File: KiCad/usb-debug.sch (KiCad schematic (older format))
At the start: 76 parts, among them IC15 TLV70018DCKT, IC16 NCP380HSNAJAAT1G, IC7 HD3SS3220, J11 632723300011, Q1 PMV32UP, T6 BSS138APW

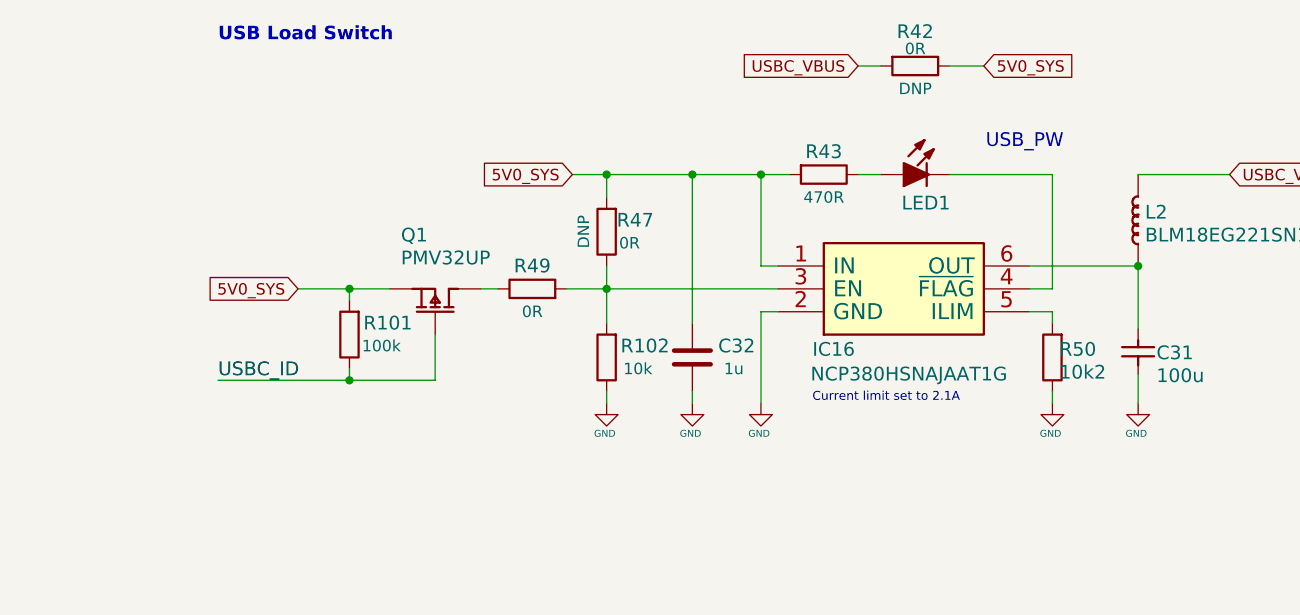
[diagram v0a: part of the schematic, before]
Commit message: Replace NCP380HS with AP22652W6-7
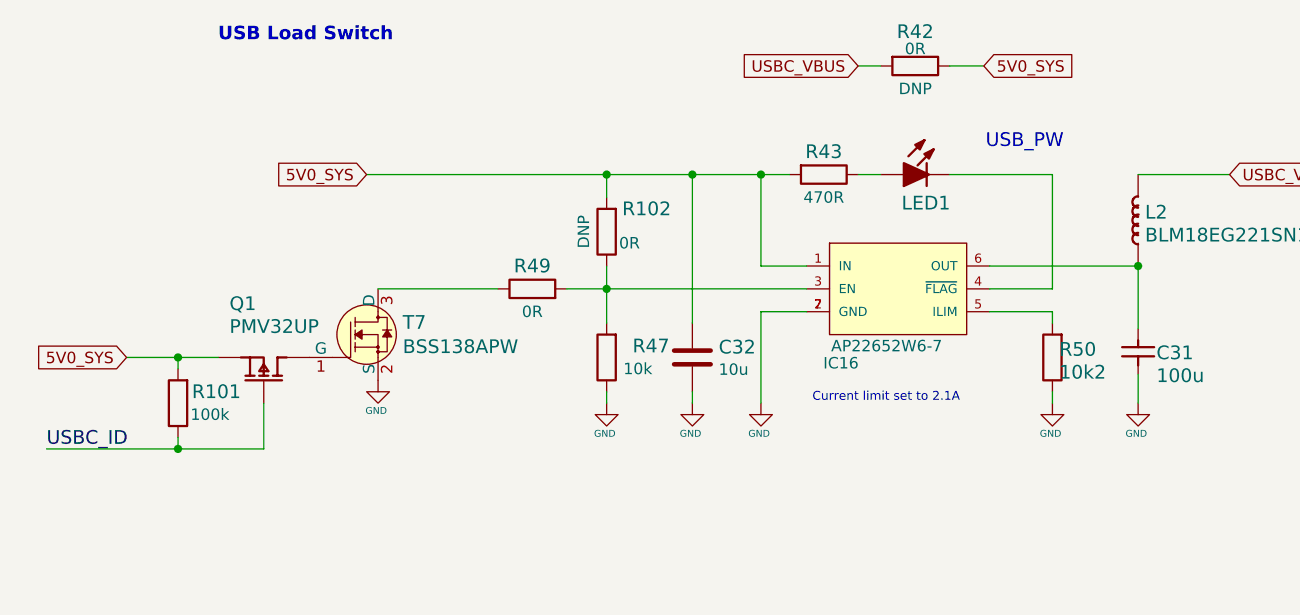
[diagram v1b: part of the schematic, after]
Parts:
- removed C32: C_1u_0402, jetson-nano-baseboard-footprints:0402-cap, symbol jetson-nano-baseboard:C_1u_0402
- removed IC16: NCP380HSNAJAAT1G, jetson-nano-baseboard-footprints:TSOP-6, symbol jetson-nano-baseboard:NCP380HSNAJAAT1G
- added C32: C_10u_0402, antmicro-footprints:0402-cap, symbol antmicroCapacitors0402:C_10u_0402
- added IC16: AP22652W6-7, antmicro-footprints:SOT-23-6, symbol antmicroPMICPowerDistributionSwitchesLoadDrivers:AP22652W6-7
- added T7: BSS138APW, jetson-nano-baseboard-footprints:SC70-3, symbol jetson-nano-baseboard:BSS138APW
- renumbered R47 to R102, R102 to R47
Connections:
- net 5V0_SYS: now also C32.1, IC16.1 (IN)
- net GND: now also C32.2, IC16.2 (GND), IC16.7 (GND), T7.2 (S)
- net at R50.2: now also IC16.5 (ILIM)
- net at C31.2, L2.1 (P): now also IC16.6 (OUT)
- net at Q1.3 (D): now also T7.1 (G); no longer R49.1
- net at LED1.K: now also IC16.4 (~FLAG~)
- net at R102.1, R47.2, R49.2: now also IC16.3 (EN)
- new net: R49.1, T7.3 (D)
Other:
- moved on the sheet: Q1, R101
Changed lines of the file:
@@
 Text Notes 4108 8992 0    60   ~ 0
 USB_PW
-Text Label 750  10000 0    60   ~ 0
+Text Label 0    10300 0    60   ~ 0
 USBC_ID
 Text Label 12600 5075 1    70   ~ 0
@@
 Text Label 4500 5650 0    60   ~ 0
 OTG_USB_VBUS
-Text GLabel 1100 9600 0    50   Input ~ 0
+Text GLabel 350  9900 0    50   Input ~ 0
 5V0_SYS
-Text GLabel 2300 9100 0    50   Input ~ 0
+Text GLabel 1400 9100 0    50   Input ~ 0
 5V0_SYS
 Text GLabel 5175 9100 2    50   Input ~ 0
@@
 $EndComp
 $Comp
-L jetson-nano-baseboard:NCP380HSNAJAAT1G IC16
-U 1 1 5E710326
-P 3800 9600
-F 0 "IC16" H 3350 9300 60  0000 L BNN
-F 1 "NCP380HSNAJAAT1G" H 3342 9192 60  0000 L BNN
-F 2 "jetson-nano-baseboard-footprints:TSOP-6" H 3350 9100 60  0001 C CNN
-F 3 "" H 3350 9100 60  0001 C CNN
-F 4 "ON Semiconductor" V 1400 8707 60  0001 C CNN "Manufacturer"
-F 5 "NCP380HSNAJAAT1G" H -34116 -14968 50  0001 C CNN "MPN"
-	1    3800 9600
-	1    0    0    -1
-$EndComp
-$Comp
 L jetson-nano-baseboard:LED LED1
 U 1 1 5E710325
@@
 L jetson-nano-baseboard:PMOS Q1
 U 1 1 5E710318
-P 1700 9600
-F 0 "Q1" V 1900 9750 60  0000 R TNN
-F 1 "PMV32UP" V 1800 9750 60  0000 R TNN
-F 2 "jetson-nano-baseboard-footprints:SOT-23s" H 1800 9750 60  0001 C CNN
-F 3 "" H 1800 9750 60  0001 C CNN
-F 4 "PMV32UP" H -34116 -14968 50  0001 C CNN "MPN"
-F 5 "NXP" H -34116 -14968 50  0001 C CNN "Manufacturer"
-	1    1700 9600
+P 950 9900
+F 0 "Q1" V 1150 10050 60  0000 R TNN
+F 1 "PMV32UP" V 1050 10050 60  0000 R TNN
+F 2 "jetson-nano-baseboard-footprints:SOT-23s" H 1050 10050 60  0001 C CNN
+F 3 "" H 1050 10050 60  0001 C CNN
+F 4 "PMV32UP" H -34866 -14668 50  0001 C CNN "MPN"
+F 5 "NXP" H -34866 -14668 50  0001 C CNN "Manufacturer"
+	1    950  9900
 	0    -1   -1   0
 $EndComp
@@
 	5725 5950 5575 5950
 Wire Wire Line
-	1700 10000 1700 9800
-Wire Wire Line
-	3200 9700 3125 9700
+	950  10300 950  10100
 Wire Wire Line
 	3125 9700 3125 10100
 Connection ~ 2450 9600
-Wire Wire Line
-	2450 9600 3200 9600
-Wire Wire Line
-	2300 9100 2450 9100
 Connection ~ 2450 9100
-Wire Wire Line
-	3200 9500 3125 9500
 Wire Wire Line
 	3125 9500 3125 9100
 Connection ~ 3125 9100
-Wire Wire Line
-	4300 9600 4400 9600
 Wire Wire Line
 	4400 9600 4400 9100
@@
 $EndComp
 Wire Wire Line
-	4300 9700 4400 9700
-Wire Wire Line
 	4775 9975 4775 10100
-Wire Wire Line
-	4300 9500 4775 9500
 Wire Wire Line
 	4775 9500 4775 9775
@@
 L jetson-nano-baseboard:R_100k_0402 R101
 U 1 1 629AECD1
-P 1325 9800
-F 0 "R101" V 1375 9525 60  0000 L CNN
-F 1 "R_100k_0402" H 1325 9650 60  0001 C CNN
-F 2 "jetson-nano-baseboard-footprints:0402-res" H 1525 10000 60  0001 L CNN
-F 3 "" H 1325 9800 50  0001 C CNN
-F 4 "VISHAY" H 1525 10200 60  0001 L CNN "Manufacturer"
-F 5 "CRCW0402100KFKEDHP" H 1525 10100 60  0001 L CNN "MPN"
-F 6 "100k" V 1275 9575 50  0000 L CNN "Val"
-	1    1325 9800
+P 575 10100
+F 0 "R101" V 625 9825 60  0000 L CNN
+F 1 "R_100k_0402" H 575 9950 60  0001 C CNN
+F 2 "jetson-nano-baseboard-footprints:0402-res" H 775 10300 60  0001 L CNN
+F 3 "" H 575 10100 50  0001 C CNN
+F 4 "VISHAY" H 775 10500 60  0001 L CNN "Manufacturer"
+F 5 "CRCW0402100KFKEDHP" H 775 10400 60  0001 L CNN "MPN"
+F 6 "100k" V 525 9875 50  0000 L CNN "Val"
+	1    575  10100
 	0    -1   -1   0
 $EndComp
 Wire Wire Line
-	750  10000 1325 10000
-Wire Wire Line
-	1100 9600 1325 9600
-Wire Wire Line
-	1325 9950 1325 10000
-Connection ~ 1325 10000
-Wire Wire Line
-	1325 10000 1700 10000
-Wire Wire Line
-	1325 9650 1325 9600
-Connection ~ 1325 9600
-Wire Wire Line
-	1325 9600 1500 9600
+	0    10300 575  10300
+Wire Wire Line
+	350  9900 575  9900
+Wire Wire Line
+	575  10250 575  10300
+Connection ~ 575  10300
+Wire Wire Line
+	575  10300 950  10300
+Wire Wire Line
+	575  9950 575  9900
+Connection ~ 575  9900
+Wire Wire Line
+	575  9900 750  9900
 $Comp
 L jetson-nano-baseboard:R_0R_0402 R49
@@
 Wire Wire Line
 	2275 9600 2450 9600
-Wire Wire Line
-	1900 9600 1975 9600
-$Comp
-L jetson-nano-baseboard:R_10k_0402 R102
-U 1 1 62A1B644
-P 2450 9900
-F 0 "R102" V 2500 9625 60  0000 L CNN
-F 1 "R_10k_0402" H 2450 9750 60  0001 C CNN
-F 2 "jetson-nano-baseboard-footprints:0402-res" H 2650 10100 60  0001 L CNN
-F 3 "" H 2450 9900 50  0001 C CNN
-F 4 "VISHAY" H 2650 10300 60  0001 L CNN "Manufacturer"
-F 5 "CRCW040210K0FKEDHP" H 2650 10200 60  0001 L CNN "MPN"
-F 6 "10k" V 2400 9700 50  0000 L CNN "Val"
-	1    2450 9900
-	0    -1   -1   0
-$EndComp
-$Comp
-L jetson-nano-baseboard:C_1u_0402 C32
-U 1 1 62A1DA70
-P 2825 9900
-F 0 "C32" H 2550 9850 60  0000 L CNN
-F 1 "C_1u_0402" H 2825 9750 60  0001 C CNN
-F 2 "jetson-nano-baseboard-footprints:0402-cap" H 3025 10100 60  0001 L CNN
-F 3 "" H 2825 9900 50  0001 C CNN
-F 4 "TDK" H 3025 10300 60  0001 L CNN "Manufacturer"
-F 5 "C1005X6S1A105K050BC" H 3025 10200 60  0001 L CNN "MPN"
-F 6 "1u" H 2600 9950 50  0000 L CNN "Val"
-	1    2825 9900
-	-1   0    0    1
-$EndComp
 $Comp
 L jetson-nano-baseboard:GND #GND_0102
@@
 Wire Wire Line
 	2450 9600 2450 9750
-Wire Wire Line
-	2450 10050 2450 10100
-$Comp
-L jetson-nano-baseboard:R_0R_0402 R47
-U 1 1 62A9631F
-P 2450 9350
-F 0 "R47" V 2500 9225 60  0000 C CNN
-F 1 "R_0R_0402" H 2450 9200 60  0001 C CNN
-F 2 "jetson-nano-baseboard-footprints:0402-res" H 2650 9550 60  0001 L CNN
-F 3 "" H 2450 9350 50  0001 C CNN
-F 4 "PANASONIC" H 2650 9750 60  0001 L CNN "Manufacturer"
-F 5 "ERJ2GE0R00X" H 2650 9650 60  0001 L CNN "MPN"
-F 6 "0R" V 2400 9250 50  0000 C CNN "Val"
-F 7 "DNP" H 2450 9450 50  0000 C CNN "DNP"
-	1    2450 9350
-	0    -1   -1   0
-$EndComp
 Wire Wire Line
 	2450 9100 2450 9200
@@
 Wire Wire Line
 	4400 10100 4400 10050
+Wire Wire Line
+	1450 9600 1975 9600
+$Comp
+L jetson-nano-baseboard:GND #GND_0152
+U 1 1 61861FAC
+P 1450 10000
+F 0 "#GND_0152" H 1450 10000 20  0001 C CNN
+F 1 "GND" H 1442 9867 30  0000 C CNN
+F 2 "" H 1450 10000 70  0001 C CNN
+F 3 "" H 1450 10000 70  0001 C CNN
+	1    1450 10000
+	1    0    0    -1
+$EndComp
+Wire Wire Line
+	1400 9100 2450 9100
+$Comp
+L jetson-nano-baseboard:BSS138APW T?
+U 1 1 617C458B
+P 1450 9800
+AR Path="/608DC6E9/617C458B" Ref="T?"  Part="1"
+AR Path="/608DF3E5/617C458B" Ref="T7"  Part="1"
+F 0 "T7" H 1558 9853 60  0000 L CNN
+F 1 "BSS138APW" H 1558 9747 60  0000 L CNN
+F 2 "jetson-nano-baseboard-footprints:SC70-3" H 1650 10000 60  0001 L CNN
+F 3 "" H 1650 10100 60  0001 L CNN
+F 4 "BSS138PW" H 1650 10300 60  0001 L CNN "MPN"
+F 5 "ON Semiconductor" H 1650 10900 60  0001 L CNN "Manufacturer"
+	1    1450 9800
+	1    0    0    -1
+$EndComp
+$Comp
+L antmicroPMICPowerDistributionSwitchesLoadDrivers:AP22652W6-7 IC16
+U 1 1 618DCEF2
+P 3725 9600
+F 0 "IC16" H 3475 9275 50  0000 C CNN
+F 1 "AP22652W6-7" H 3675 9350 50  0000 C CNN
+F 2 "antmicro-footprints:SOT-23-6" H 3725 9350 50  0001 C CNN
+F 3 "https://www.diodes.com/assets/Datasheets/AP22652_53_52A_53A.pdf" H 3725 9600 50  0001 C CNN
+F 4 "Diodes Incorporated " H 3725 9250 50  0001 C CNN "Manufacturer"
+F 5 "" H 3725 9600 50  0000 C CNN "DNP"
+	1    3725 9600
+	1    0    0    -1
+$EndComp
+Wire Wire Line
+	3125 9500 3325 9500
+Wire Wire Line
+	2450 9600 3325 9600
+Wire Wire Line
+	3125 9700 3325 9700
+Wire Wire Line
+	4125 9600 4400 9600
+Wire Wire Line
+	4125 9500 4775 9500
+Wire Wire Line
+	4125 9700 4400 9700
+$Comp
+L antmicroCapacitors0402:C_10u_0402 C32
+U 1 1 619B98FA
+P 2825 9900
+F 0 "C32" H 2940 9945 60  0000 L CNN
+F 1 "C_10u_0402" H 2825 9750 60  0001 C CNN
+F 2 "antmicro-footprints:0402-cap" H 3025 10100 60  0001 L CNN
+F 3 "" H 2825 9900 50  0001 C CNN
+F 4 "MURATA" H 3025 10300 60  0001 L CNN "Manufacturer"
+F 5 "GRM155R60J106ME44D" H 3025 10200 60  0001 L CNN "MPN"
+F 6 "10u" H 2940 9847 50  0000 L CNN "Val"
+	1    2825 9900
+	1    0    0    -1
+$EndComp
+Wire Wire Line
+	2450 10050 2450 10100
+$Comp
+L jetson-nano-baseboard:R_10k_0402 R47
+U 1 1 62A1B644
+P 2450 9900
+F 0 "R47" V 2500 9625 60  0000 L CNN
+F 1 "R_10k_0402" H 2450 9750 60  0001 C CNN
+F 2 "jetson-nano-baseboard-footprints:0402-res" H 2650 10100 60  0001 L CNN
+F 3 "" H 2450 9900 50  0001 C CNN
+F 4 "VISHAY" H 2650 10300 60  0001 L CNN "Manufacturer"
+F 5 "CRCW040210K0FKEDHP" H 2650 10200 60  0001 L CNN "MPN"
+F 6 "10k" V 2400 9700 50  0000 L CNN "Val"
+	1    2450 9900
+	0    -1   -1   0
+$EndComp
+$Comp
+L jetson-nano-baseboard:R_0R_0402 R102
+U 1 1 62A9631F
+P 2450 9350
+F 0 "R102" V 2550 9175 60  0000 C CNN
+F 1 "R_0R_0402" H 2450 9200 60  0001 C CNN
+F 2 "jetson-nano-baseboard-footprints:0402-res" H 2650 9550 60  0001 L CNN
+F 3 "" H 2450 9350 50  0001 C CNN
+F 4 "PANASONIC" H 2650 9750 60  0001 L CNN "Manufacturer"
+F 5 "ERJ2GE0R00X" H 2650 9650 60  0001 L CNN "MPN"
+F 6 "0R" V 2400 9250 50  0000 C CNN "Val"
+F 7 "DNP" H 2450 9450 50  0000 C CNN "DNP"
+	1    2450 9350
+	0    -1   -1   0
+$EndComp
 $EndSCHEMATC
